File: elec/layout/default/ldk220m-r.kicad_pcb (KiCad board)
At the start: 2 copper layers, 225.7 x 100.8 mm, 5 parts

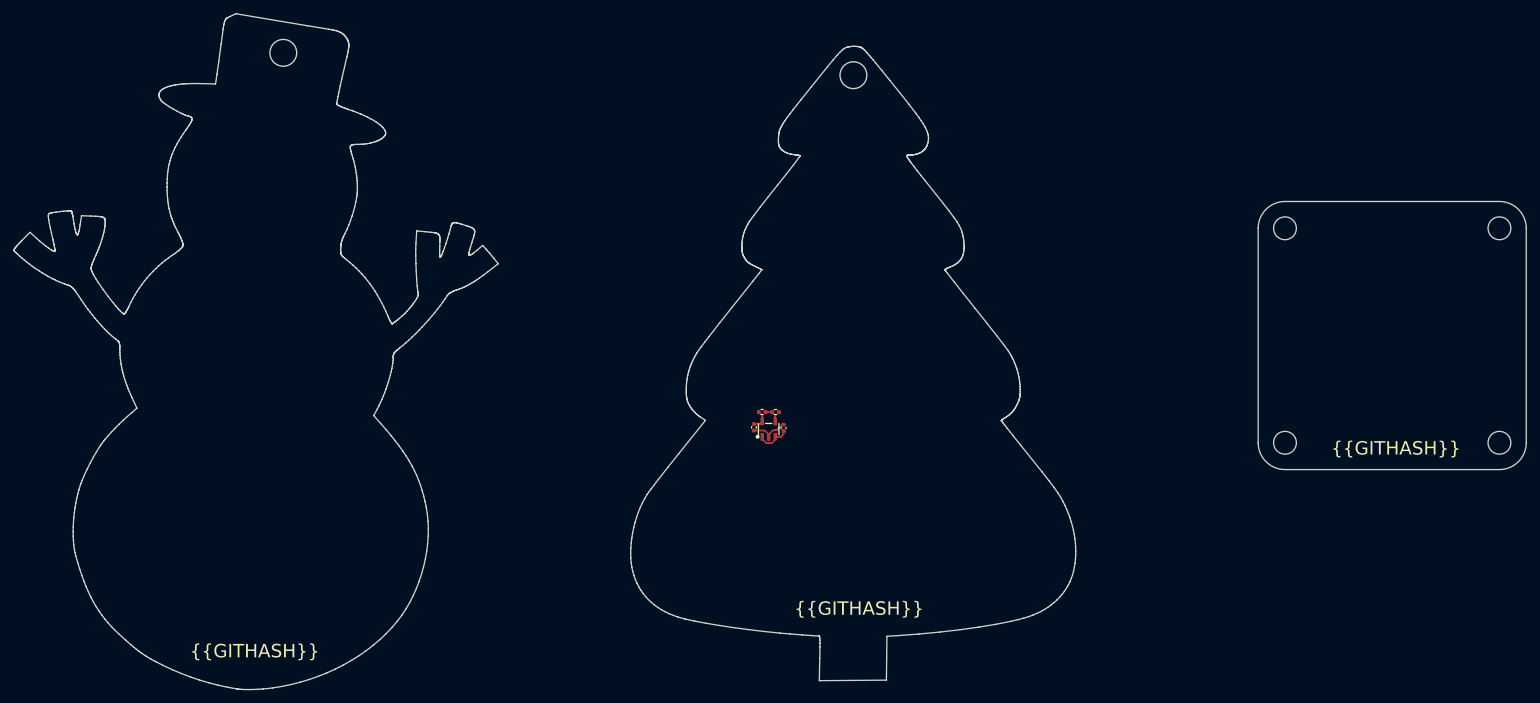
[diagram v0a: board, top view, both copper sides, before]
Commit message: removed the dreaded snowman, saved layout with kicad V8
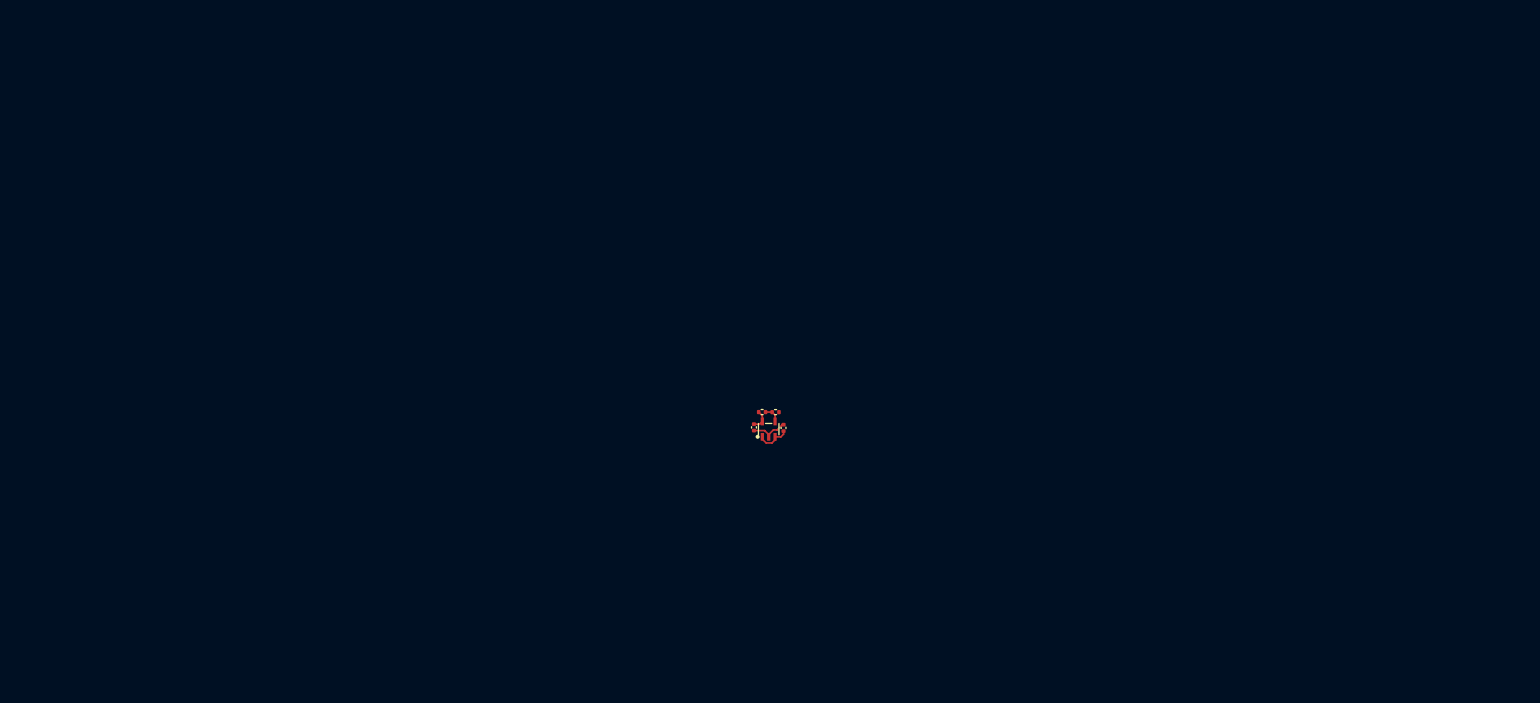
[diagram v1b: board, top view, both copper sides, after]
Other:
- board outline removed
- board text removed: "{{GITHASH}}"

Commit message: Ran build to update atopile addresses in layout
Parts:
- C1, C2: value Multilayer Ceramic Capacitors MLCC - SMD/SMT 1uF 6.3V 0402 RoHS -> 1µF ±10% 25V X5R; footprint lib:C0402 -> atopile:C0402-b3ef17
- R1: value Chip Resistor - Surface Mount 18KOhms ±5% 1/16W 0402 RoHS -> 1kΩ ±1% 62.5mW; footprint lib:R0402 -> atopile:R0402-56259e
- R2: value Chip Resistor - Surface Mount 10KOhms ±5% 1/16W 0402 RoHS -> 1kΩ ±1% 62.5mW; footprint lib:R0402 -> atopile:R0402-56259e
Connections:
- net vcc renamed IN
- net vcc-1 renamed hv
